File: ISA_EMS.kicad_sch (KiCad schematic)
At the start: 51 parts, among them J1 ISA BUS, J2 EMS Address, U1 74HCT573, U10 74HCT32, U11 74HCT04, U12 74LS245, U13 AS6C4008-55PCN, U14 AS6C4008-55PCN, U15 AS6C4008-55PCN, U16 AS6C4008-55PCN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

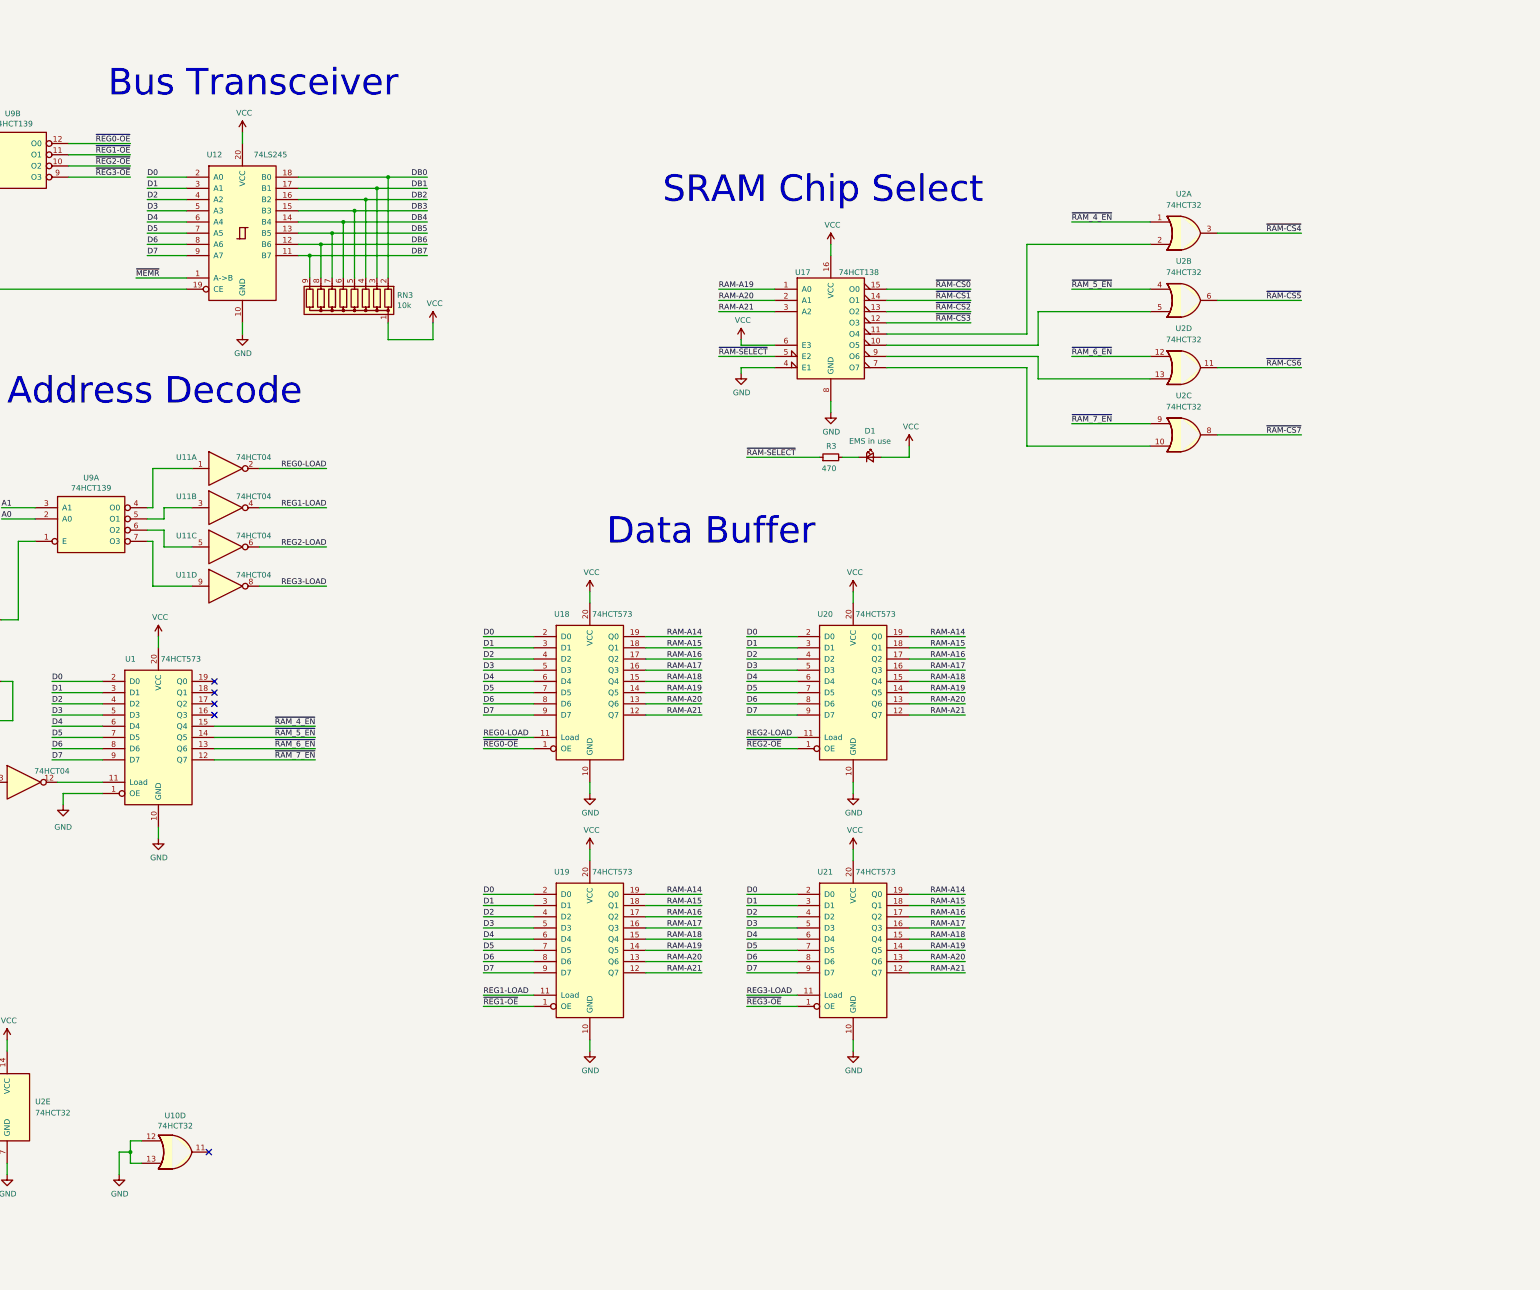
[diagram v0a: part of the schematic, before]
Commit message: Disable upper memory per-window
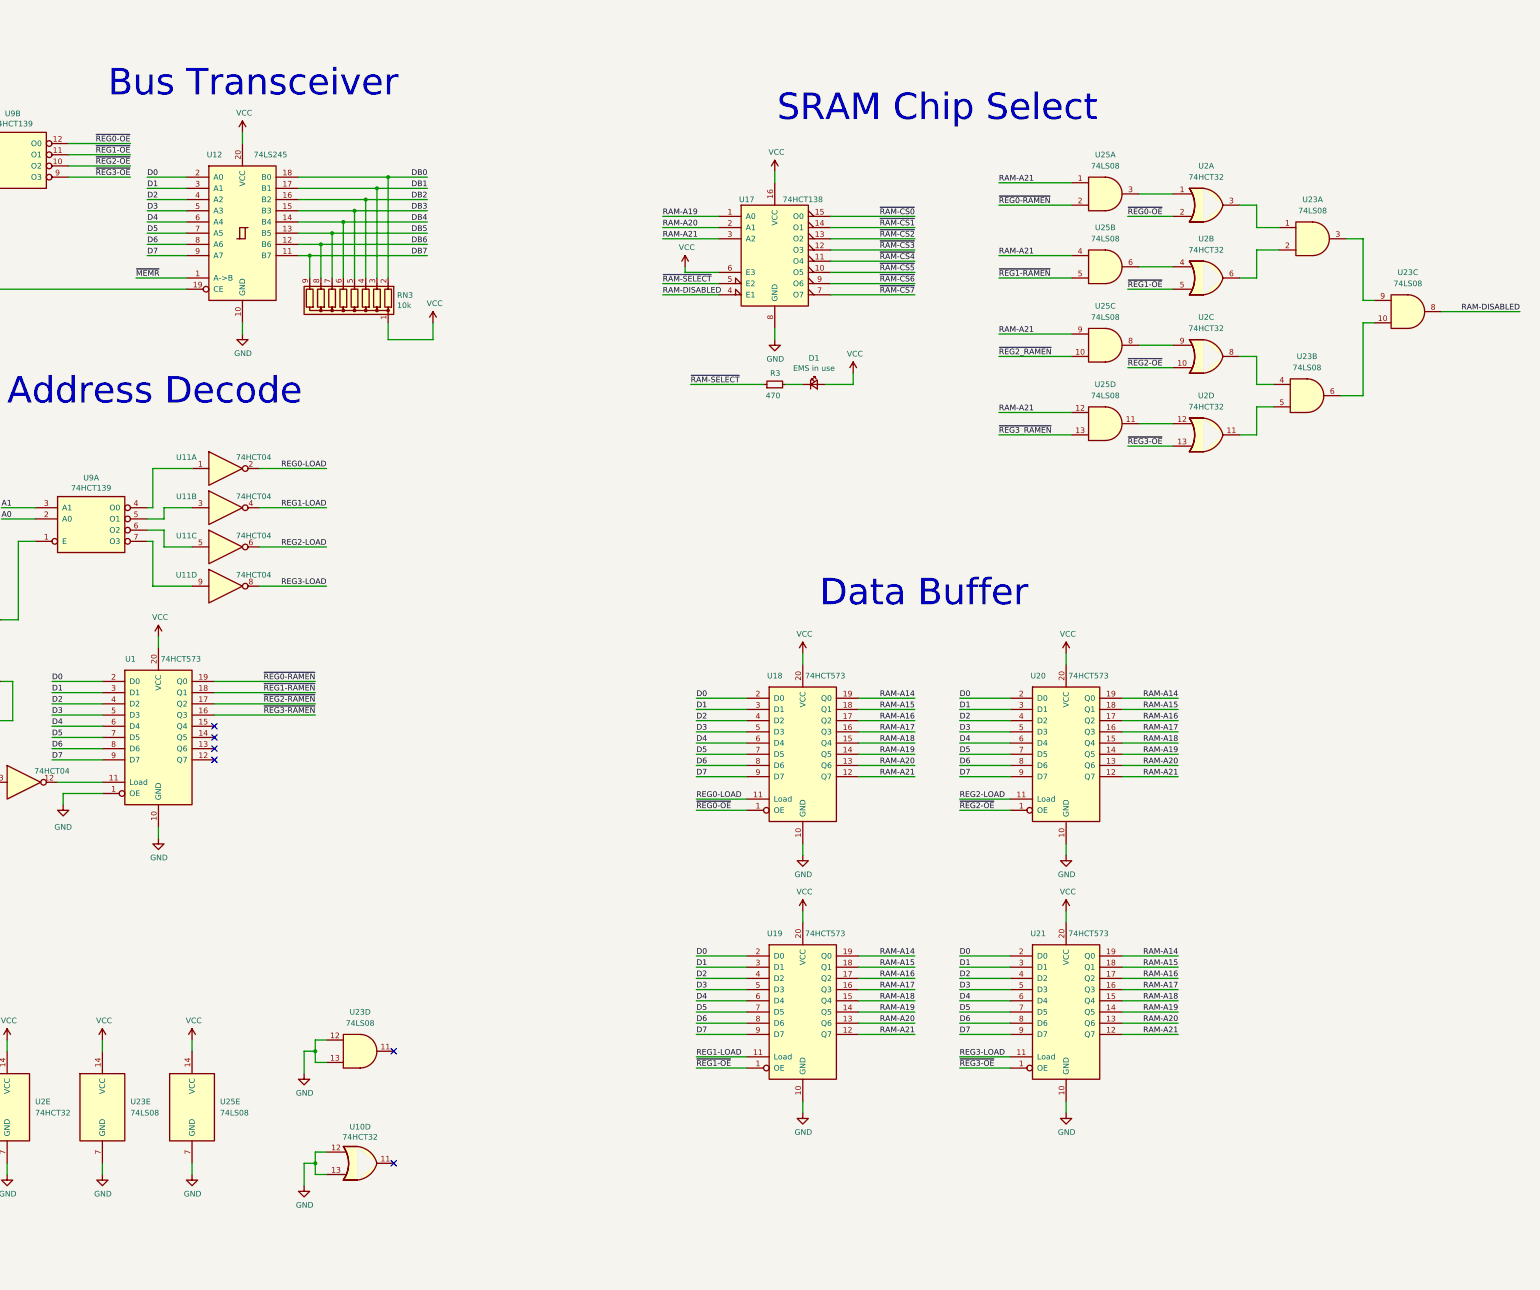
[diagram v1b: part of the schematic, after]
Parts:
- added U23, U25: 74LS08, symbol 74xx:74LS08
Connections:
- net GND: now also U23.12, U23.13, U23.7 (GND), U25.7 (GND); no longer U17.4 (E1)
- net RAM-A21: now also U25.1, U25.12, U25.4, U25.9
- net VCC: now also U23.14 (VCC), U25.14 (VCC)
- net ~{RAM-CS4}: now also U17.11 (O4); no longer U2.3
- net ~{RAM-CS5}: now also U17.10 (O5); no longer U2.6
- net ~{RAM-CS6}: now also U17.9 (O6); no longer U2.11
- net ~{RAM-CS7}: now also U17.7 (O7); no longer U2.8
- net ~{REG0-OE}: now also U2.2
- net ~{REG1-OE}: now also U2.5
- net ~{REG2-OE}: now also U2.10
- net ~{REG3-OE}: now also U2.13
- net ~{REG3-RAMEN}: now reaches U1.16 (Q3)
- net ~{REG2-RAMEN}: now reaches U1.17 (Q2)
- net ~{REG1-RAMEN}: now reaches U1.18 (Q1)
- net ~{REG1-RAMEN}: now also U25.5
- net ~{REG0-RAMEN}: now reaches U1.19 (Q0)
- net ~{REG0-RAMEN}: now also U25.2
- net ~{RAM_4_EN}: no longer names the net of U2.1
- net ~{RAM_4_EN}: now also U25.3; no longer U1.15 (Q4)
- net ~{RAM_5_EN}: no longer names the net of U2.4
- net ~{RAM_5_EN}: now also U25.6; no longer U1.14 (Q5)
- net ~{RAM_6_EN}: no longer names the net of U2.12
- net ~{RAM_6_EN}: now also U25.11; no longer U1.13 (Q6)
- net ~{RAM_7_EN}: no longer names the net of U2.9
- net ~{RAM_7_EN}: now also U25.8; no longer U1.12 (Q7)
- new net: U2.8, U23.4
- new net: U2.6, U23.2
- new net: U2.11, U23.5
- new net: U23.10, U23.6
- new net: U2.3, U23.1
- new net: U23.3, U23.9
- new net RAM-DISABLED: U17.4 (E1), U23.8
- new net ~{REG2_RAMEN}: U25.10
- new net ~{REG3_RAMEN}: U25.13
- no-connect marks 18 -> 19
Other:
- moved on the sheet: D1, R3, U10D, U17, U18, U19, U20, U21, U2A, U2B, U2C, U2D

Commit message: Upda type of some ICs
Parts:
- added C1, C2: 100nF, Capacitor_THT:C_Disc_D6.0mm_W2.5mm_P5.00mm, symbol Device:C_Small
- U17: value 74HCT138 -> 74HC138
- U2: value 74HCT32 -> 74HC32
- U23, U25: value 74LS08 -> 74HC08
- U9: value 74HCT139 -> 74HC139
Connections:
- net GND: now also C1.2, C2.2
- net VCC: now also C1.1, C2.1

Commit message: Updated schematic
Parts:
- removed J2: EMS Address, Connector_PinHeader_2.54mm:PinHeader_2x04_P2.54mm_Vertical, symbol Connector_Generic:Conn_02x04_Odd_Even
- removed RN2: 10k, Resistor_THT:R_Array_SIP5, symbol Device:R_Network04
- added J2: EMS Address, Connector_PinHeader_2.54mm:PinHeader_2x03_P2.54mm_Vertical, symbol Connector_Generic:Conn_02x03_Odd_Even
- added RN1: 10K, Resistor_THT:R_Array_SIP4, symbol Device:R_Network03
- U2, U23, U25: footprint (none) -> Package_DIP:DIP-14_W7.62mm_LongPads
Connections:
- net GND: now also J2.1 (Pin_1), J2.3 (Pin_3), J2.5 (Pin_5)
- net JP1: now also J2.2 (Pin_2), RN1.2 (R1)
- net JP2: now also J2.4 (Pin_4), RN1.3 (R2)
- net VCC: now also RN1.1 (common)
- net JP4 renamed JP3
- net JP3: now also J2.6 (Pin_6), RN1.4 (R3)

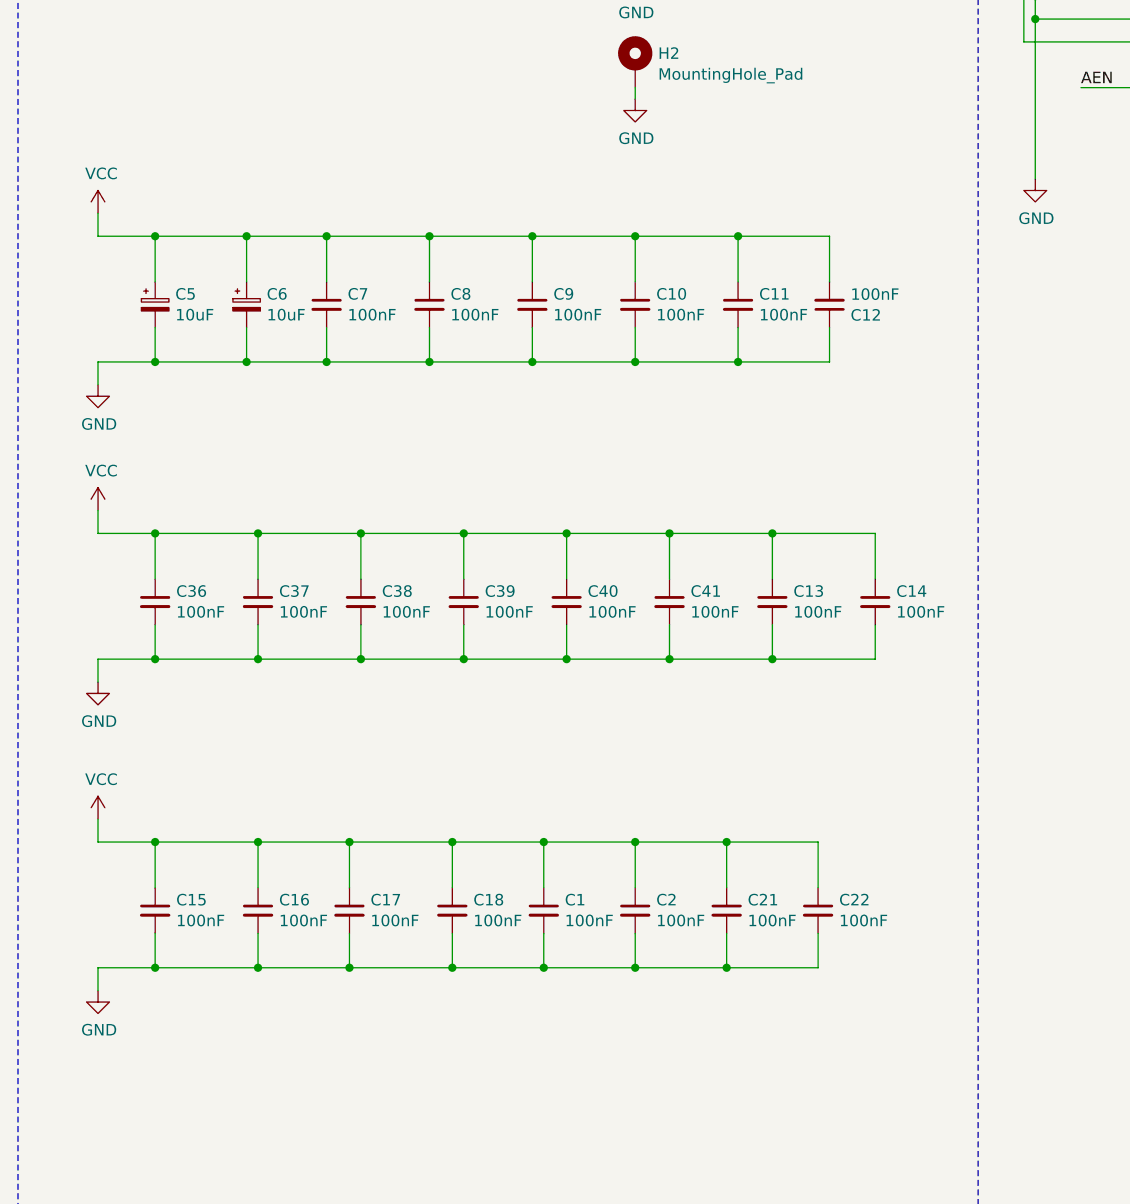
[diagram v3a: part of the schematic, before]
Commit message: Replace components on board
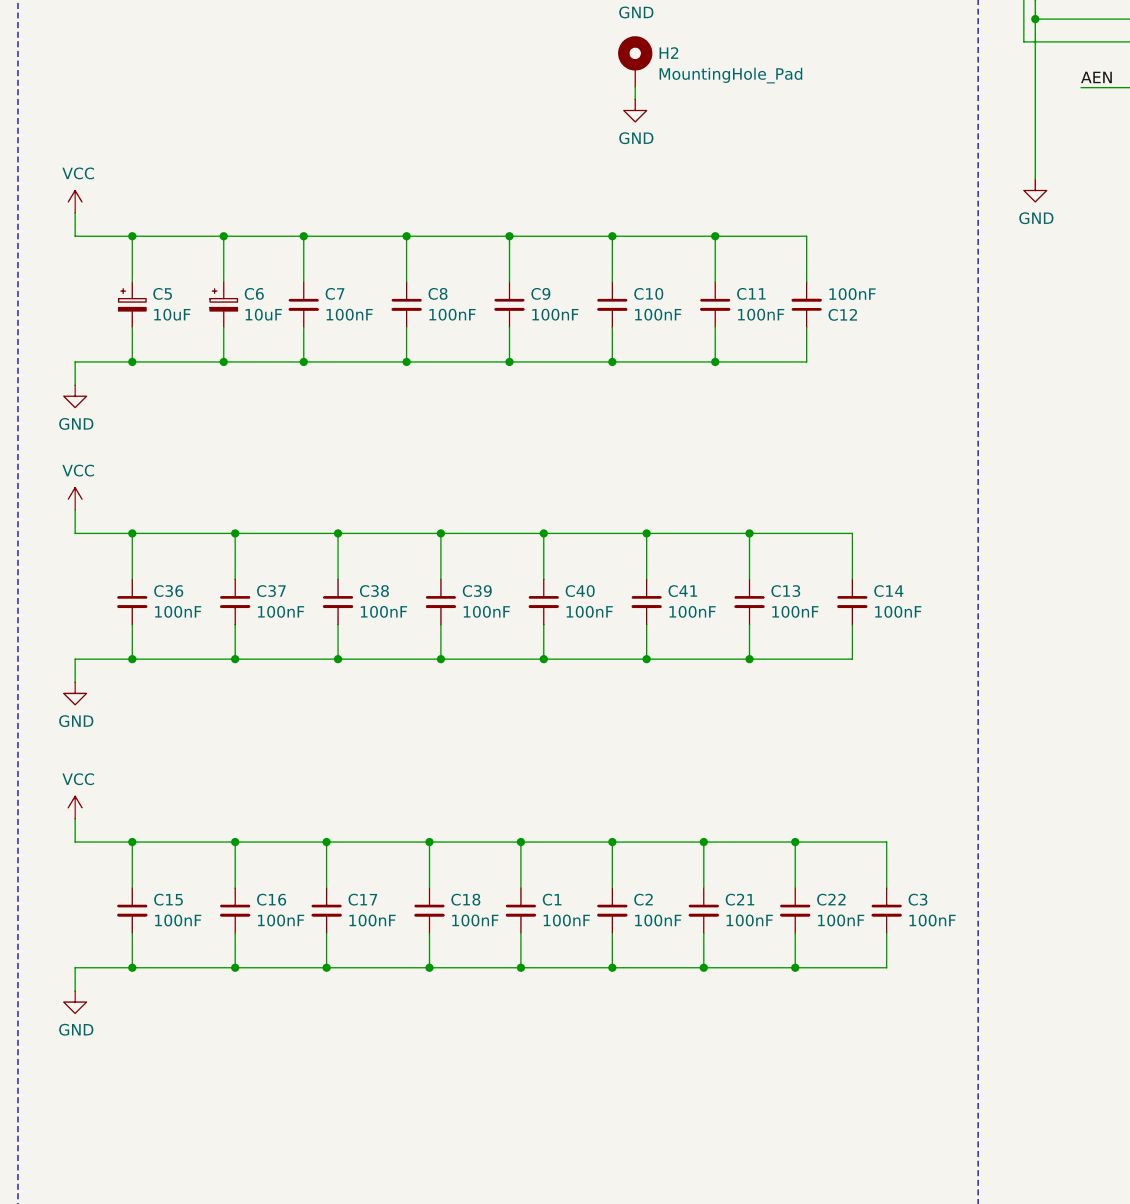
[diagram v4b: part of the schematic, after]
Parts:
- added C3: 100nF, Capacitor_SMD:C_1206_3216Metric_Pad1.33x1.80mm_HandSolder, symbol Device:C_Small
- C1, C10, C11, C12, C13, C14, C15, C16, C17, C18, C2, C21, C22, C36, C37, C38, C39, C40, C41, C7, C8, C9: footprint Capacitor_THT:C_Disc_D6.0mm_W2.5mm_P5.00mm -> Capacitor_SMD:C_1206_3216Metric_Pad1.33x1.80mm_HandSolder
- U1, U12, U18, U19, U20, U21, U7, U8: footprint Package_DIP:DIP-20_W7.62mm_LongPads -> Package_DIP:DIP-20_W7.62mm
- U10, U11, U2, U23, U25: footprint Package_DIP:DIP-14_W7.62mm_LongPads -> Package_DIP:DIP-14_W7.62mm
- U17, U9: footprint Package_DIP:DIP-16_W7.62mm_LongPads -> Package_DIP:DIP-16_W7.62mm
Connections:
- net GND: now also C3.2
- net VCC: now also C3.1
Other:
- moved on the sheet: C1, C10, C11, C12, C13, C14, C15, C16, C17, C18, C2, C21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
